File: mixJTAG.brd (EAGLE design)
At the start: 100 x 80 mm, 58 parts, among them J1 PLUG-A, J2 CON_HEADER_2X08, Q1 NPN, U1 RCLAMP0544M, U10 SRV05-4, U2 93LC56B, U3 FT2232HLLQFP, U4 XC2C32A-6VQ44C, U5 TC2117-800MA, U6 MCP601, U7 SRV05-4, U8 SRV05-4, U9 SRV05-4, X1 12MHz

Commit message: first layout
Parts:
- removed C26: 100n, rcl:C0805
- removed Q1: NPN, bb_transistor:SOT23
- removed R6, R8: 10k, rcl:R0805
- removed R7: 2k, rcl:R0805
- removed R9: 200R, rcl:R0805
- removed U10: SRV05-4, bb_tvs:SOT23-6
- added J4: (no value), bb_ml:ML20
- added L4: 600R0.5A, others:R0805
- added PCB1: PCB_DP_RECTANGLE-50X100, bb_pcb:DP10050_V1
- added RA5: 50R, bb_ra:EXBV8V
- C10, C11, C18, C25: value 100n -> 4.7u; device rcl:C0805 -> rcl:B/3528-21R
- C17, C21: value 4.7u -> 100n; device rcl:CT3216 -> rcl:C0805
- C23: value 4.7u -> 100n
- C5, C6: device rcl:CT3216 -> rcl:B/3528-21R
- C8: value (none) -> 100n; device rcl:CT3216 -> rcl:C0805
- J2: value CON_HEADER_2X08 -> CON_HEADER_1X03-PTH; device bb_pinheader:M2X8 -> bb_pinheader:M1X3
- J3: value (none) -> CON_HEADER_2X08; device bb_ml:ML20 -> bb_pinheader:M2X8
- R4: value 10k -> 2k
- R5: value 10k -> 200R
- RA1: value 50R -> 10k
- U1: value RCLAMP0544M -> SRV05-4; device bb_tvs:MSOP10 -> bb_tvs:SOT23-6
- U4: value XC2C32A-6VQ44C -> TC2117-800MA; device bb_xc2c32a:VQ-44 -> bb_ldo:SOT223
- U5: value TC2117-800MA -> XC2C32A-6VQ44C; device bb_ldo:SOT223 -> bb_xc2c32a:VQ-44
- U6: value MCP601 -> SRV05-4; device bb_op:SO08 -> bb_tvs:SOT23-6
- moved LED1 138.5 mm to (57.1, 40.6), turned to 90 degrees
- moved C25 113.7 mm to (77.5, 42.7), turned to 90 degrees
- moved R5 109.9 mm to (51.8, 40.6)
- moved C15 102.1 mm to (33.0, 29.2), flipped to the bottom, turned to 90 degrees
- moved C7 97.5 mm to (27.9, 28.2), flipped to the bottom, turned to 90 degrees
- moved C10 97.4 mm to (40.6, 29.2), flipped to the bottom, turned to 270 degrees
- moved C22 87.5 mm to (54.1, 21.6), flipped to the bottom
- moved R4 87.4 mm to (33.0, 34.8), turned to 90 degrees
- moved C13 87.2 mm to (36.8, 29.2), flipped to the bottom, turned to 90 degrees
- moved C20 87.1 mm to (52.8, 25.4), flipped to the bottom, turned to 90 degrees
- moved R1 85.1 mm to (25.1, 9.40), flipped to the bottom, turned to 270 degrees
- moved C12 82.1 mm to (35.8, 7.62), flipped to the bottom, turned to 270 degrees
- moved C19 78.8 mm to (16.5, 40.6), turned to 90 degrees
- moved C24 78.4 mm to (81.3, 43.2), turned to 270 degrees
- moved C23 77.5 mm to (65.0, 23.9), flipped to the bottom, turned to 180 degrees
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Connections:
- removed net N$7: R8.1, U6.6
- removed net N$8: Q1.1, R8.2
- removed net VCC: U10.5, U7.5, U8.5, U9.5
- new net VREF: C24.1, C25.+, J2.3, L4.2
- net +1V8: now also C10.+, C13.1, C22.1, C8.1, U5.15; no longer C10.1, C11.1, C16.1, C8.+, U4.15
- net +3V3: now also C16.1, C17.1, C18.+, C19.1, C21.1, J2.1, RA1.1, RA1.2, RA1.3, RA1.4, U4.2, U5.35, U5.7; no longer C13.1, C14.1, C18.1, C21.+, C22.1, R4.1, R5.1, R6.1, U4.35, U4.7, U5.2
- net +5V: now also U1.5; no longer Q1.3, U1.8, U6.7
- net CPLD_TCK: now also U5.11; no longer U4.11
- net CPLD_TDI: now also U5.9; no longer U4.9
- net CPLD_TDO: now also U5.24; no longer U4.24
- net CPLD_TMS: now also U5.10; no longer U4.10
- net EECS: now also RA1.5; no longer R6.2
- net EEDATA: now also R4.1; no longer R7.1
- net EESK: now also RA1.6; no longer R5.2
- net GND: now also C10.-, C11.-, C17.2, C18.-, C21.2, C25.-, C8.2, J4.10, J4.12, J4.14, J4.16, J4.18, J4.20, J4.4, J4.6, J4.8, R5.1, U1.2, U4.1, U5.17, U5.25, U5.4, U6.2; no longer C10.2, C11.2, C17.-, C18.2, C21.-, C25.2, C26.2, C8.-, J3.10, J3.12, J3.14, J3.16, J3.18, J3.20, J3.4, J3.6, J3.8, R9.1, U1.3, U10.2, U4.17, U4.25, U4.4, U5.1, U6.4
- net GPIOH0: now also U5.2; no longer U4.2
- net GPIOH1: now also U5.1; no longer U4.1
- net GPIOH2: now also U5.44; no longer U4.44
- net GPIOH3: now also U5.43; no longer U4.43
- net GPIOH4: now also U5.42; no longer U4.42
- net GPIOH5: now also U5.41; no longer U4.41
- net GPIOH6: now also U5.40; no longer U4.40
- net GPIOH7: now also U5.39; no longer U4.39
- net GPIOL0: now also U5.8; no longer U4.16
- net GPIOL1: now also U5.6; no longer U4.14
- net GPIOL2: now also U5.5; no longer U4.13
- net GPIOL3: now also U5.3; no longer U4.12
- net IN13: now also J3.10, J4.11, RA4.8; no longer J2.10, J3.11, RA3.8
- net IN14: now also J3.9, RA4.7; no longer J2.9, J3.13, RA3.7
- net IN15: now also J3.12, J4.13, RA4.6; no longer J2.12, RA3.6
- net IN28: now also J3.15, RA5.5; no longer J2.15, RA4.5
- net IN29: now also J3.16, RA5.6; no longer J2.16, RA4.6
- net IN30: now also J3.13, RA5.7; no longer J2.13, RA4.7
- net IN31: now also J3.14, J4.15, RA5.8; no longer J2.14, RA4.8
- net IN32: now also J3.11, RA4.5; no longer J2.11, RA3.5
- net IO0: now also RA2.1, U5.38, U6.1; no longer RA1.1, U4.38, U7.6
- net IO1: now also RA2.2, U5.37, U6.6; no longer RA1.2, U4.37, U7.1
- net IO10: now also RA4.3, U5.27, U8.4; no longer RA3.3, U4.27
- net IO11: now also RA4.4, U5.23, U8.3; no longer RA3.4, U4.23, U9.1
- net IO12: now also RA5.1, U5.22, U9.1; no longer RA4.1, U10.3, U10.6, U4.22
- net IO13: now also RA5.2, U5.21, U9.6; no longer RA4.2, U10.4, U4.21
- net IO14: now also RA5.3, U5.20, U9.4; no longer RA4.3, U4.20
- net IO15: now also RA5.4, U5.19, U9.3; no longer RA4.4, U10.1, U4.19
- net IO2: now also RA2.3, U5.36, U6.4; no longer RA1.3, U4.36, U7.3
- net IO3: now also RA2.4, U5.34, U6.3; no longer RA1.4, U4.34, U7.4
- net IO4: now also RA3.1, U5.33, U7.1; no longer RA2.1, U4.33, U8.6
- net IO5: now also RA3.2, U5.32, U7.6; no longer RA2.2, U4.32, U8.3, U8.4
- net IO6: now also RA3.3, U5.31, U7.4; no longer RA2.3, U4.31
- net IO7: now also RA3.4, U5.30, U7.3; no longer RA2.4, U4.30, U8.1
- net IO8: now also RA4.1, U5.29, U8.1; no longer RA3.1, U4.29, U9.3, U9.6
- net IO9: now also RA4.2, U5.28, U8.6; no longer RA3.2, U4.28, U9.4
- net N$1: now also U1.6; no longer U1.2
- net N$13: now also RA1.8; no longer R7.2
- net N$3: now also C11.+, C14.1, U4.3; no longer C17.+, C19.1, U5.3
- net N$4: now also J4.1, J4.2, L4.1; no longer J3.1, J3.2
- net N$6: now also R5.2; no longer R9.2
- net OUT10: now also J3.8, J4.9, RA3.6; no longer J2.8, RA2.6
- net OUT11: now also J3.7, RA3.5; no longer J2.7, RA2.5
- net OUT4: now also J3.2, J4.3, RA2.8; no longer J2.2, J3.3, RA1.8
- net OUT5: now also J3.1, RA2.7; no longer J2.1, J3.5, RA1.7
- net OUT6: now also J3.4, J4.5, RA2.6; no longer J2.4, J3.7, RA1.6
- net OUT7: now also J3.3, RA2.5; no longer J2.3, J3.9, RA1.5
- net OUT8: now also J3.6, J4.7, RA3.8; no longer J2.6, J3.15, RA2.8
- net OUT9: now also J3.5, RA3.7; no longer J2.5, RA2.7
- net REF: no longer C25.1, U6.3
- net TCK: now also U5.16; no longer U4.8
- net TDI: now also U5.14; no longer U4.6
- net TDO: now also U5.13; no longer U4.5
- net TGT: now also J2.2, U5.26; no longer C24.1, C26.1, Q1.2, U4.26, U6.2
- net TMS: now also U5.12; no longer U4.3
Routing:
- net +3V3: track 0.00 -> 216.8 mm, vias 0 -> 8
- net +1V8: track 0.00 -> 60.6 mm, vias 0 -> 4
- net CPLD_TCK: track 0.00 -> 48.9 mm, vias 0 -> 2
- net CPLD_TDO: track 0.00 -> 48.2 mm, vias 0 -> 2
- net CPLD_TDI: track 0.00 -> 44.5 mm, vias 0 -> 2
- net GND: track 11.8 -> 53.3 mm, vias 1 -> 0
- net CPLD_TMS: track 0.00 -> 38.5 mm, vias 0 -> 2
- net GPIOH7: track 0.00 -> 37.6 mm
- net GPIOH6: track 0.00 -> 35.4 mm
- net GPIOH5: track 0.00 -> 33.1 mm
- net EESK: track 0.00 -> 30.3 mm, vias 0 -> 2
- net GPIOH4: track 0.00 -> 30.0 mm
- net EECS: track 0.00 -> 29.4 mm
- net GPIOH3: track 0.00 -> 27.6 mm
- net TGT: track 0.00 -> 27.5 mm, vias 0 -> 1
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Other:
- board size 100 x 80 mm -> 100 x 50.8 mm

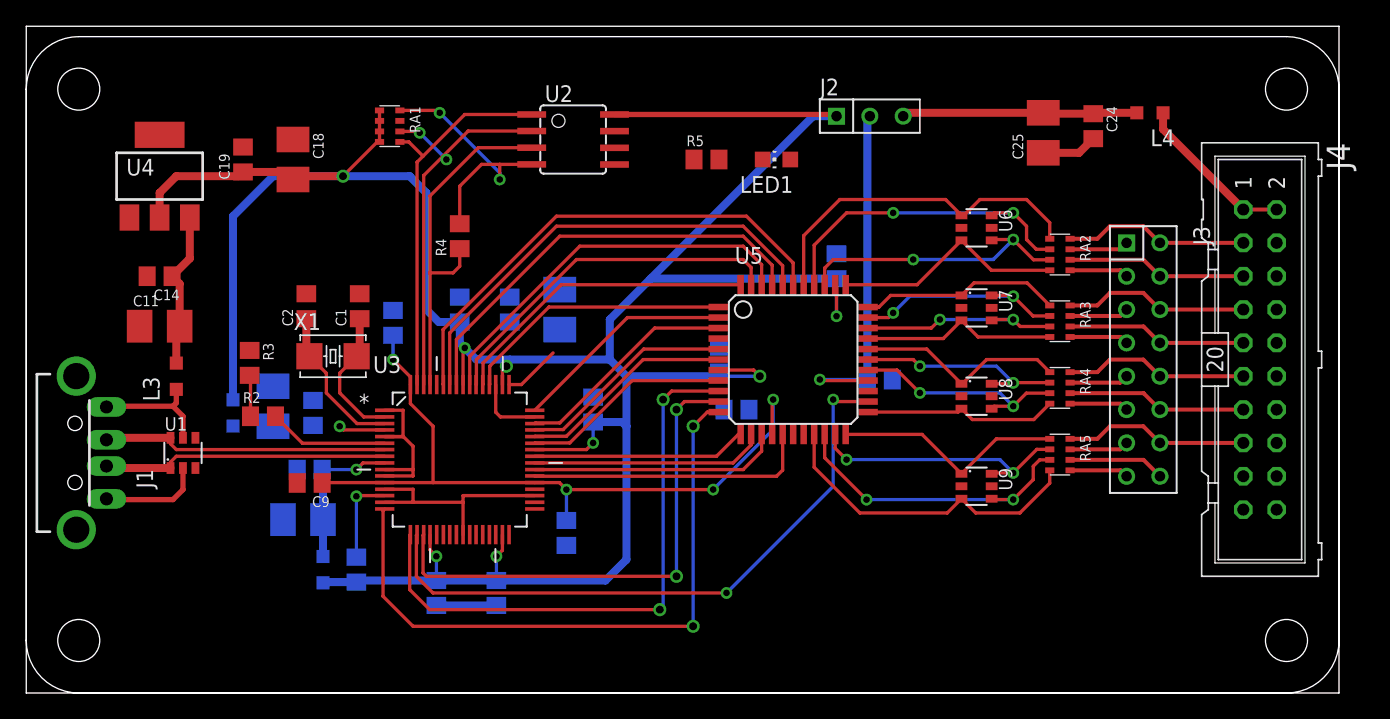
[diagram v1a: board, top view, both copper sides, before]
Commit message: change usb pad
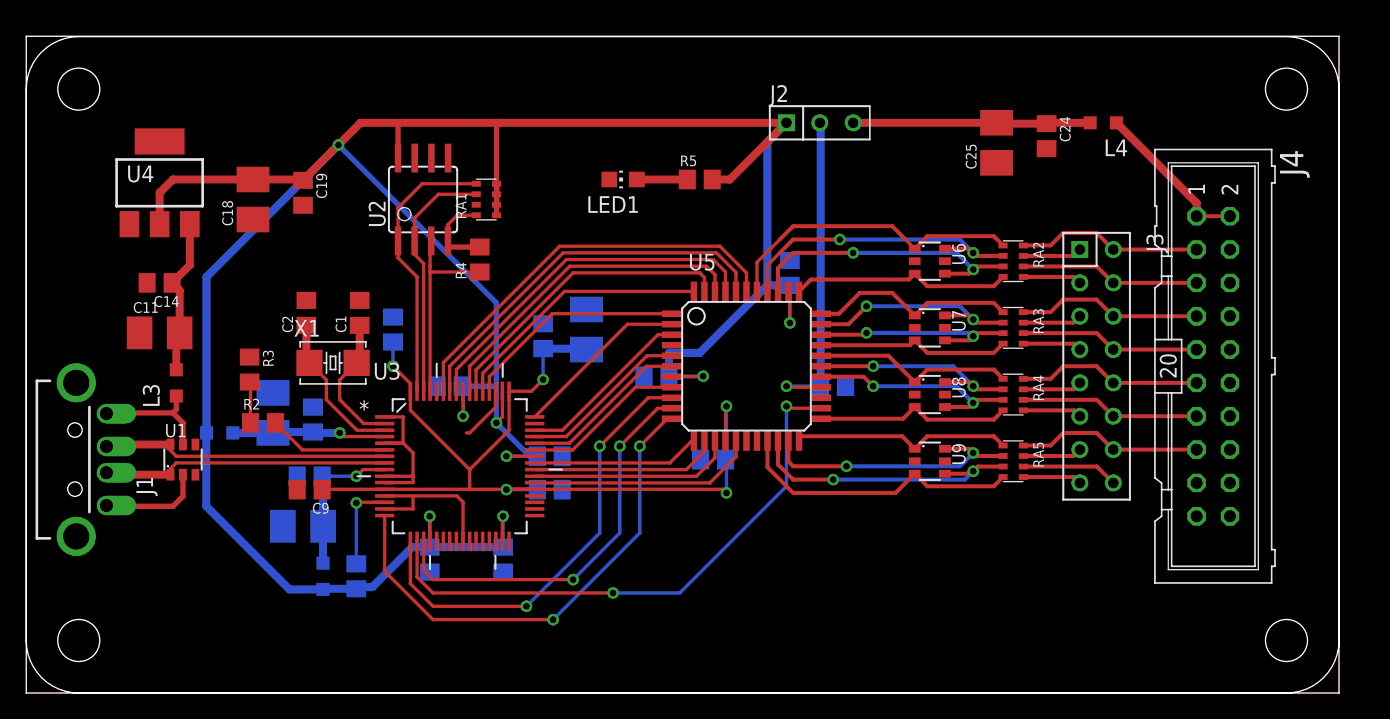
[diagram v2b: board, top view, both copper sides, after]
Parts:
- moved U2 12.3 mm to (30.2, 37.6), turned to 0 degrees
- moved LED1 11.8 mm to (45.5, 39.1)
- moved RA1 9.25 mm to (35.1, 37.6), turned to 90 degrees
- moved C15 5.89 mm to (32.3, 23.4), turned to 0 degrees
- moved C19 5.23 mm to (21.1, 38.1), turned to 270 degrees
- moved C20 4.99 mm to (48.0, 24.1), turned to 0 degrees
- moved C16 4.85 mm to (39.9, 18.0), turned to 180 degrees
- moved U6 4.37 mm to (68.8, 32.9)
- moved C18 4.31 mm to (17.3, 37.6), turned to 90 degrees
- moved C22 4.20 mm to (52.3, 17.8)
- moved U9 4.03 mm to (68.8, 17.7)
- moved U7 3.87 mm to (68.8, 27.8)
- moved J2 3.84 mm to (57.9, 43.4)
- moved C24 3.64 mm to (77.7, 42.4)
- moved C25 3.64 mm to (73.9, 41.9)
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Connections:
- net +3V3: now also R5.2; no longer LED1.A
- net GND: now also LED1.C; no longer R5.1
- net N$6: now also LED1.A, R5.1; no longer LED1.C, R5.2
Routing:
- net GND: track 53.3 -> 38.2 mm
- net +1V8: track 60.6 -> 74.4 mm, vias 4 -> 5
- net N$13: track 20.3 -> 6.58 mm, vias 2 -> 0
- net EEDATA: track 27.4 -> 15.3 mm
- net EESK: track 30.3 -> 18.9 mm, vias 2 -> 0
- net CPLD_TCK: track 48.9 -> 38.0 mm
- net CPLD_TDI: track 44.5 -> 34.3 mm
- net VPHY: track 3.54 -> 11.7 mm
- net EECS: track 29.4 -> 21.3 mm
- net CPLD_TMS: track 38.5 -> 30.7 mm
- net GPIOH7: track 37.6 -> 31.2 mm
- net GPIOH6: track 35.4 -> 29.4 mm
- net GPIOH5: track 33.1 -> 27.5 mm
- net GPIOH4: track 30.0 -> 25.3 mm
- net CPLD_TDO: track 48.2 -> 43.5 mm
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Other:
- board size 100 x 50.8 mm -> 100 x 50 mm
